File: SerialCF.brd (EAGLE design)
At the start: 101.6 x 34 mm, 4 parts, among them IC1 Z80CPU

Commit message: Finish Modularization
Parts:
- removed QG1: 6 MHz, crystal:DIL14S
- added LED1: AC, led:LED5MM
- added R1: 1k, eagle-ltspice:0207/10
- added R2: 560, resistor:0204/7
- added SV1: SERIAL, con-lstb:MA04-1
- added SV2: IDE PATA CF Card, con-lstb:MA20-2
- added V1, V2: 74HC00N, 74ttl-din:DIL14
- IC1: value Z80CPU -> XR-16C550P; device zilog:DIL40 -> exar:DIL40
- moved U$1 65.4 mm to (95.2, 12.7)
- moved IC1 31.9 mm to (34.3, 19.1), turned to 180 degrees
- moved JP1 1.27 mm to (73.7, 0.00)
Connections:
- removed net CLOCK: IC1.6, JP1.63, QG1.8
- removed net N$10: IC1.22, JP1.57
- removed net N$14: IC1.21, JP1.55
- removed net N$16: IC1.20, JP1.59
- removed net N$22: IC1.23, JP1.67
- removed net N$8: IC1.19, JP1.61
- removed net N$9: IC1.18, JP1.71
- new net !RD: IC1.21, SV2.25
- new net !WR: IC1.18, SV2.23
- new net +UB: V2.14
- new net -UB: V2.7
- new net IOCS1: SV2.37, V2.11
- new net N$11: IC1.11, SV1.1
- new net N$13: IC1.15, IC1.9
- new net N$15: IC1.10, SV1.2
- new net N$17: V1.13, V1.8
- new net N$18: IC1.14, V2.3
- new net N$19: JP1.59, V1.12, V1.2
- new net N$2: LED1.K, SV2.39
- new net N$20: R1.1, SV2.38
- new net N$3: LED1.A, R2.1
- new net N$4: V1.3, V2.2
- new net N$5: V2.1, V2.6
- new net N$6: V2.13, V2.8
- new net N$7: V1.11, V2.12
- new net RESET: IC1.35, V1.6
- net !RESET: now also SV2.1, V1.4, V1.5; no longer IC1.26
- net A0: now also IC1.28, SV2.35; no longer IC1.30
- net A1: now also IC1.27, SV2.33; no longer IC1.31
- net A10: no longer IC1.40
- net A11: no longer IC1.1
- net A12: no longer IC1.2
- net A13: no longer IC1.3
- net A14: no longer IC1.4
- net A15: no longer IC1.5
- net A2: now also IC1.26, SV2.36; no longer IC1.32
- net A3: no longer IC1.33
- net A4: no longer IC1.34
- net A5: no longer IC1.35
- net A6: now also V2.10, V2.4, V2.5, V2.9; no longer IC1.36
- net A7: now also V1.1, V1.10, V1.9; no longer IC1.37
- net A8: no longer IC1.38
- net A9: no longer IC1.39
- net D0: now also IC1.1, SV2.17; no longer IC1.14
- net D1: now also IC1.2, SV2.15; no longer IC1.15
- net D2: now also IC1.3, SV2.13; no longer IC1.12
- net D3: now also IC1.4, SV2.11; no longer IC1.8
- net D4: now also IC1.5, SV2.9; no longer IC1.7
- net D5: now also IC1.6, SV2.7; no longer IC1.9
- net D6: now also IC1.7, SV2.5; no longer IC1.10
- net D7: now also IC1.8, SV2.3; no longer IC1.13
- net GND: now also IC1.19, IC1.20, IC1.22, IC1.25, SV1.4, SV2.19, SV2.2, SV2.22, SV2.24, SV2.26, SV2.30, SV2.40, V1.7; no longer IC1.29, QG1.7
- net N$1: now also IC1.16, JP1.63; no longer IC1.27, JP1.75
- net VCC: now also IC1.12, IC1.13, IC1.37, IC1.38, IC1.39, IC1.40, R1.2, R2.2, SV1.3, SV2.20, V1.14; no longer IC1.11, IC1.16, IC1.17, IC1.25, JP1.69, JP1.73, JP1.77, QG1.14
- net WAIT: now also SV2.27; no longer IC1.24
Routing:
- net N$16: track 103.1 -> 0.00 mm, vias 1 -> 0
- net N$9: track 93.5 -> 0.00 mm, vias 1 -> 0
- net N$22: track 88.1 -> 0.00 mm
- net !RD: track 0.00 -> 87.0 mm, vias 0 -> 1
- net !WR: track 0.00 -> 83.0 mm, vias 0 -> 1
- net N$4: track 0.00 -> 78.9 mm, vias 0 -> 1
- net N$7: track 0.00 -> 74.7 mm, vias 0 -> 2
- net N$8: track 70.6 -> 0.00 mm, vias 1 -> 0
- net N$14: track 68.4 -> 0.00 mm, vias 2 -> 0
- net N$10: track 68.0 -> 0.00 mm, vias 2 -> 0
- net A7: track 28.0 -> 88.8 mm
- net N$19: track 0.00 -> 59.0 mm
- net D6: track 25.8 -> 84.7 mm, vias 0 -> 1
- net N$18: track 0.00 -> 57.4 mm, vias 0 -> 2
- net N$20: track 0.00 -> 57.1 mm, vias 0 -> 1
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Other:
- board size 101.6 x 34 mm -> 101.6 x 50.5 mm
- board text added: "+"
- board text added: "-"
- board text added: "CPD-80 Serial/CF V1"
- board text added: "RX"
- board text added: "TX"
- board text removed: "CPD-80 CPU V1"

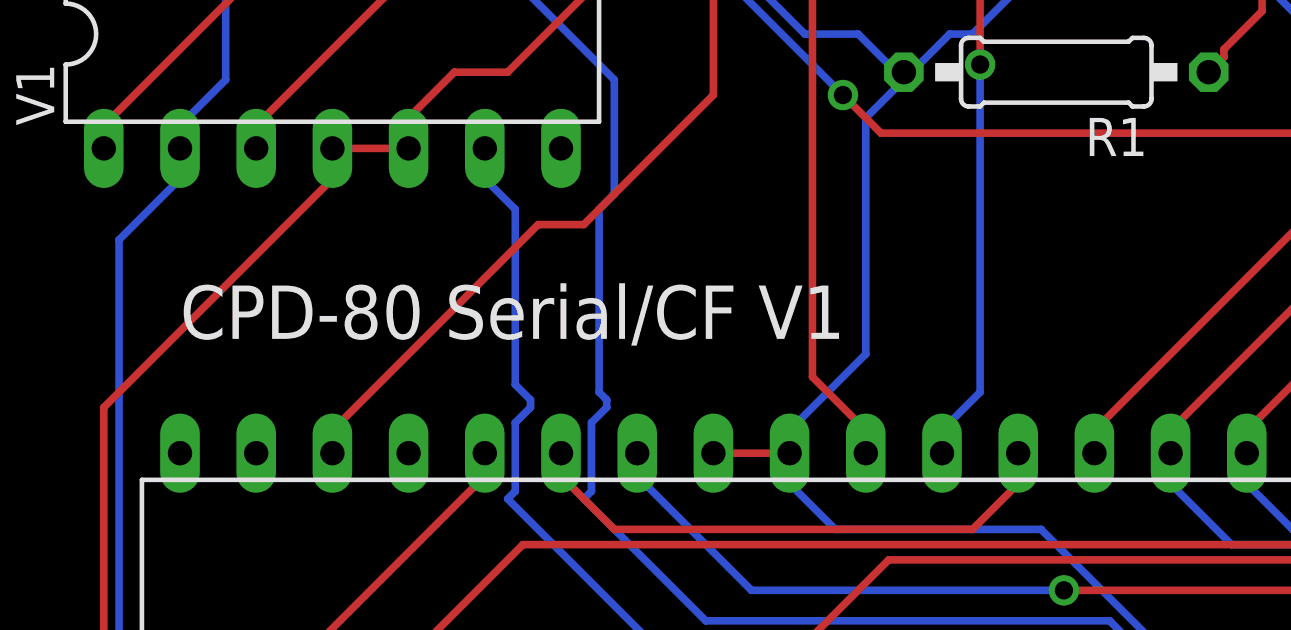
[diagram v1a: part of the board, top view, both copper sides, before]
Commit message: Update names and font
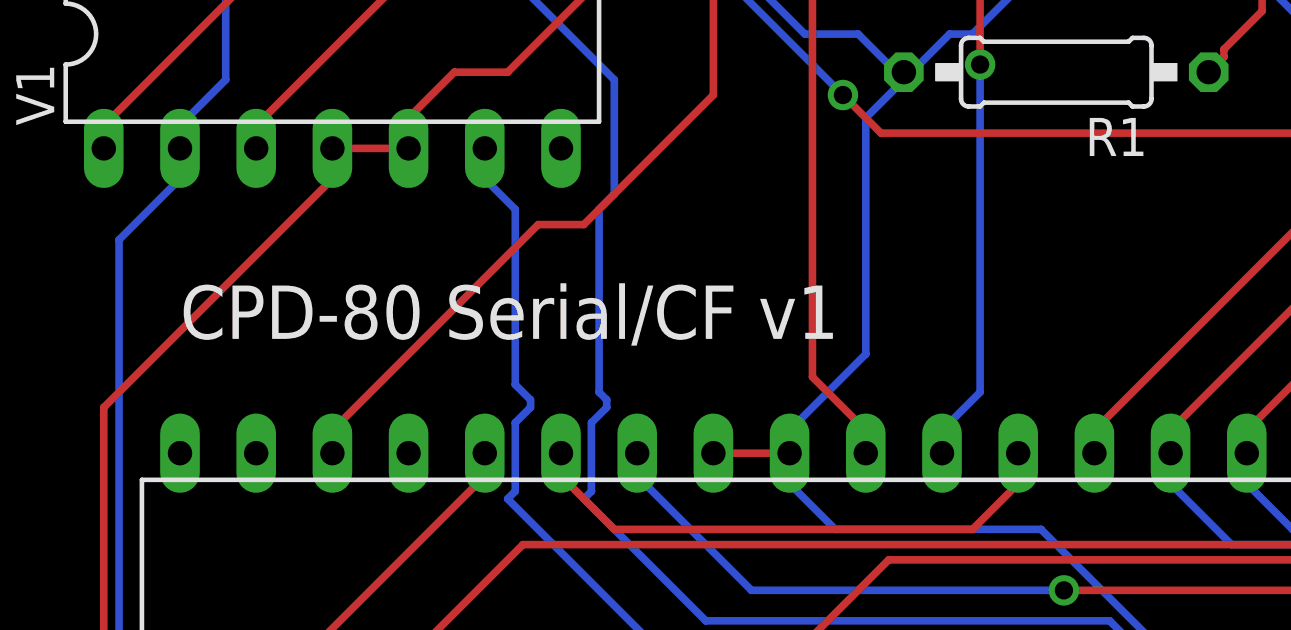
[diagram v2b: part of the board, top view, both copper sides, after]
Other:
- board text added: "CPD-80 Serial/CF v1"
- board text removed: "CPD-80 Serial/CF V1"
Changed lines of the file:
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@@
 <wire x1="104.12" y1="50.47" x2="2.54" y2="50.47" width="0" layer="20"/>
 <wire x1="2.54" y1="50.47" x2="2.54" y2="0" width="0" layer="20"/>
-<text x="33.02" y="48.26" size="1.778" layer="27">RX</text>
-<text x="35.56" y="48.26" size="1.778" layer="27">TX</text>
-<text x="38.735" y="48.26" size="1.778" layer="27">+</text>
-<text x="41.91" y="48.26" size="1.778" layer="27">-</text>
-<text x="10.16" y="30.48" size="1.778" layer="21">CPD-80 Serial/CF V1</text>
+<text x="33.02" y="48.26" size="1.524" layer="27" font="fixed">RX</text>
+<text x="36.195" y="48.26" size="1.524" layer="27" font="fixed">TX</text>
+<text x="39.37" y="48.26" size="1.524" layer="27" font="fixed">+</text>
+<text x="41.91" y="48.26" size="1.524" layer="27" font="fixed">-</text>
+<text x="10.16" y="30.48" size="1.778" layer="21" font="fixed">CPD-80 Serial/CF v1</text>
 <rectangle x1="50.5333" y1="30.5435" x2="50.8635" y2="30.5689" layer="21"/>
 <rectangle x1="50.3301" y1="30.5689" x2="50.9397" y2="30.5943" layer="21"/>

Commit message: Add Interrupt connection for 16550
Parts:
- added R3: 100k, resistor:0207/2V
- added R4: 3.3k, resistor:0207/2V
- added T1: BC547, transistor:TO92
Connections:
- new net N$10: IC1.30, R3.1
- new net N$8: R3.2, T1.2
- new net N$9: JP1.73, R4.1, T1.3
- net GND: now also T1.1
- net VCC: now also R4.2
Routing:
- net N$9: track 0.00 -> 68.7 mm, vias 0 -> 2
- net N$10: track 0.00 -> 34.7 mm, vias 0 -> 1
- net D1: track 74.3 -> 84.8 mm, vias 1 -> 3
- net N$8: track 0.00 -> 6.00 mm
- net VCC: track 185.7 -> 191.0 mm, vias 0 -> 1
- net N$18: track 57.4 -> 59.5 mm, vias 2 -> 3
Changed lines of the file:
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@@
 <element name="V2" library="74ttl-din" package="DIL14" value="74HC00N" x="80.01" y="31.75"/>
 <element name="U$1" library="bfl" package="OSHW2" value="" x="95.25" y="12.7"/>
+<element name="T1" library="transistor" package="TO92" value="BC547" x="71.12" y="17.78"/>
+<element name="R3" library="resistor" package="0207/2V" value="100k" x="64.77" y="21.59"/>
+<element name="R4" library="resistor" package="0207/2V" value="3.3k" x="63.5" y="16.51"/>
 </elements>
 <signals>
@@
 <wire x1="94.488" y1="22.352" x2="94.742" y2="22.352" width="0.254" layer="1"/>
 <wire x1="83.82" y1="11.684" x2="94.488" y2="22.352" width="0.254" layer="1"/>
-<wire x1="58.674" y1="11.684" x2="83.82" y2="11.684" width="0.254" layer="1"/>
+<wire x1="58.674" y1="11.684" x2="65.8368" y2="11.684" width="0.254" layer="1"/>
+<wire x1="65.8368" y1="11.684" x2="83.82" y2="11.684" width="0.254" layer="1"/>
 <wire x1="58.42" y1="11.43" x2="58.674" y2="11.684" width="0.254" layer="1"/>
 <wire x1="36.83" y1="6.604" x2="36.83" y2="6.35" width="0.254" layer="1"/>
@@
 <wire x1="30.48" y1="25.654" x2="32.004" y2="24.13" width="0.254" layer="16"/>
 <wire x1="30.48" y1="26.67" x2="30.48" y2="25.654" width="0.254" layer="16"/>
+<contactref element="R4" pad="2"/>
+<wire x1="64.9224" y1="16.002" x2="64.9224" y2="16.4592" width="0.254" layer="16"/>
+<wire x1="65.8368" y1="15.0876" x2="64.9224" y2="16.002" width="0.254" layer="16"/>
+<wire x1="65.8368" y1="13.0302" x2="65.8368" y2="15.0876" width="0.254" layer="16"/>
+<wire x1="65.8368" y1="11.684" x2="65.8368" y2="13.0302" width="0.254" layer="1"/>
+<wire x1="64.9224" y1="16.4592" x2="64.77" y2="16.51" width="0.254" layer="16"/>
+<wire x1="65.8368" y1="11.6586" x2="65.8368" y2="11.684" width="0.254" layer="1"/>
+<via x="65.8368" y="13.0302" extent="1-16" drill="0.6096"/>
 </signal>
 <signal name="GND">
@@
 <vertex x="104.14" y="49.53"/>
 </polygon>
+<contactref element="T1" pad="1"/>
 </signal>
 <signal name="A0">
@@
 <wire x1="91.694" y1="15.24" x2="100.33" y2="6.604" width="0.254" layer="16"/>
 <wire x1="74.676" y1="15.24" x2="91.694" y2="15.24" width="0.254" layer="16"/>
-<wire x1="66.294" y1="15.24" x2="74.676" y2="15.24" width="0.254" layer="1"/>
-<wire x1="55.88" y1="25.654" x2="66.294" y2="15.24" width="0.254" layer="1"/>
+<wire x1="66.294" y1="15.24" x2="73.3806" y2="15.24" width="0.254" layer="1"/>
+<wire x1="73.3806" y1="15.24" x2="74.676" y2="15.24" width="0.254" layer="1"/>
 <wire x1="55.88" y1="26.67" x2="55.88" y2="25.654" width="0.254" layer="1"/>
 <via x="74.676" y="15.24" extent="1-16" drill="0.6096"/>
+<wire x1="57.3786" y1="25.6032" x2="55.7784" y2="25.6032" width="0.254" layer="1"/>
+<wire x1="59.8932" y1="23.0886" x2="57.3786" y2="25.6032" width="0.254" layer="1"/>
+<wire x1="67.437" y1="23.0886" x2="59.8932" y2="23.0886" width="0.254" layer="1"/>
+<wire x1="67.6656" y1="22.86" x2="67.437" y2="23.0886" width="0.254" layer="1"/>
+<wire x1="69.4944" y1="21.0312" x2="67.6656" y2="22.86" width="0.254" layer="16"/>
+<wire x1="71.3232" y1="21.0312" x2="69.4944" y2="21.0312" width="0.254" layer="1"/>
+<wire x1="73.3806" y1="18.9738" x2="71.3232" y2="21.0312" width="0.254" layer="1"/>
+<wire x1="73.3806" y1="15.24" x2="73.3806" y2="18.9738" width="0.254" layer="1"/>
+<wire x1="55.7784" y1="25.6032" x2="55.88" y2="26.67" width="0.254" layer="1"/>
+<via x="67.6656" y="22.86" extent="1-16" drill="0.6096"/>
+<via x="69.4944" y="21.0312" extent="1-16" drill="0.6096"/>
 </signal>
 <signal name="D2">
@@
 <wire x1="39.624" y1="22.098" x2="29.21" y2="22.098" width="0.254" layer="16"/>
 <wire x1="58.166" y1="22.098" x2="39.624" y2="22.098" width="0.254" layer="1"/>
-<wire x1="72.644" y1="22.098" x2="58.166" y2="22.098" width="0.254" layer="16"/>
-<wire x1="77.47" y1="26.924" x2="72.644" y2="22.098" width="0.254" layer="16"/>
+<wire x1="77.47" y1="26.924" x2="73.1647" y2="22.6187" width="0.254" layer="16"/>
+<wire x1="73.1647" y1="22.6187" x2="72.644" y2="22.098" width="0.254" layer="16"/>
 <wire x1="77.47" y1="27.94" x2="77.47" y2="26.924" width="0.254" layer="16"/>
 <via x="39.624" y="22.098" extent="1-16" drill="0.6096"/>
 <via x="58.166" y="22.098" extent="1-16" drill="0.6096"/>
+<wire x1="72.2376" y1="23.5458" x2="73.1647" y2="22.6187" width="0.254" layer="16"/>
+<wire x1="72.009" y1="23.5458" x2="72.2376" y2="23.5458" width="0.254" layer="16"/>
+<wire x1="70.4088" y1="21.9456" x2="72.009" y2="23.5458" width="0.254" layer="16"/>
+<wire x1="67.2084" y1="21.9456" x2="70.4088" y2="21.9456" width="0.254" layer="1"/>
+<wire x1="66.5226" y1="22.6314" x2="67.2084" y2="21.9456" width="0.254" layer="1"/>
+<wire x1="58.7502" y1="22.6314" x2="66.5226" y2="22.6314" width="0.254" layer="1"/>
+<wire x1="58.293" y1="22.1742" x2="58.7502" y2="22.6314" width="0.254" layer="1"/>
+<wire x1="58.293" y1="22.1742" x2="58.166" y2="22.098" width="0.254" layer="1"/>
+<via x="70.4088" y="21.9456" extent="1-16" drill="0.6096"/>
 </signal>
 <signal name="N$17">
@@
 <via x="50.8" y="39.116" extent="1-16" drill="0.6096"/>
 </signal>
+<signal name="N$8">
+<contactref element="T1" pad="2"/>
+<contactref element="R3" pad="2"/>
+<wire x1="67.6656" y1="19.8882" x2="71.0946" y2="19.8882" width="0.254" layer="1"/>
+<wire x1="66.0654" y1="21.4884" x2="67.6656" y2="19.8882" width="0.254" layer="1"/>
+<wire x1="71.0946" y1="19.8882" x2="71.12" y2="19.685" width="0.254" layer="1"/>
+<wire x1="66.0654" y1="21.4884" x2="66.04" y2="21.59" width="0.254" layer="1"/>
+</signal>
+<signal name="N$9">
+<contactref element="T1" pad="3"/>
+<contactref element="R4" pad="1"/>
+<contactref element="JP1" pad="73"/>
+<wire x1="63.3222" y1="16.6878" x2="62.4078" y2="16.6878" width="0.254" layer="1"/>
+<wire x1="64.2366" y1="17.6022" x2="63.3222" y2="16.6878" width="0.254" layer="1"/>
+<wire x1="69.723" y1="17.6022" x2="64.2366" y2="17.6022" width="0.254" layer="1"/>
+<wire x1="62.4078" y1="16.6878" x2="62.23" y2="16.51" width="0.254" layer="1"/>
+<wire x1="69.723" y1="17.6022" x2="69.85" y2="17.78" width="0.254" layer="1"/>
+<wire x1="12.573" y1="6.1722" x2="11.43" y2="6.1722" width="0.254" layer="1"/>
+<wire x1="13.716" y1="5.0292" x2="12.573" y2="6.1722" width="0.254" layer="1"/>
+<wire x1="21.9456" y1="5.0292" x2="13.716" y2="5.0292" width="0.254" layer="1"/>
+<wire x1="22.86" y1="4.1148" x2="21.9456" y2="5.0292" width="0.254" layer="1"/>
+<wire x1="22.86" y1="3.429" x2="22.86" y2="4.1148" width="0.254" layer="1"/>
+<wire x1="23.7744" y1="2.5146" x2="22.86" y2="3.429" width="0.254" layer="1"/>
+<wire x1="29.4894" y1="2.5146" x2="23.7744" y2="2.5146" width="0.254" layer="1"/>
+<wire x1="30.6324" y1="3.6576" x2="29.4894" y2="2.5146" width="0.254" layer="1"/>
+<wire x1="30.6324" y1="4.3434" x2="30.6324" y2="3.6576" width="0.254" layer="1"/>
+<wire x1="31.5468" y1="5.2578" x2="30.6324" y2="4.3434" width="0.254" layer="1"/>
+<wire x1="32.2326" y1="5.2578" x2="31.5468" y2="5.2578" width="0.254" layer="1"/>
+<wire x1="33.147" y1="6.1722" x2="32.2326" y2="5.2578" width="0.254" layer="1"/>
+<wire x1="33.147" y1="6.858" x2="33.147" y2="6.1722" width="0.254" layer="1"/>
+<wire x1="35.6616" y1="9.3726" x2="33.147" y2="6.858" width="0.254" layer="1"/>
+<wire x1="37.0332" y1="10.7442" x2="35.6616" y2="9.3726" width="0.254" layer="16"/>
+<wire x1="37.0332" y1="12.573" x2="37.0332" y2="10.7442" width="0.254" layer="16"/>
+<wire x1="40.4622" y1="16.002" x2="37.0332" y2="12.573" width="0.254" layer="16"/>
+<wire x1="61.722" y1="16.002" x2="40.4622" y2="16.002" width="0.254" layer="1"/>
+<wire x1="62.23" y1="16.51" x2="61.722" y2="16.002" width="0.254" layer="1"/>
+<wire x1="11.43" y1="6.1722" x2="11.43" y2="6.35" width="0.254" layer="1"/>
+<via x="35.6616" y="9.3726" extent="1-16" drill="0.6096"/>
+<via x="40.4622" y="16.002" extent="1-16" drill="0.6096"/>
+</signal>
+<signal name="N$10">
+<contactref element="R3" pad="1"/>
+<contactref element="IC1" pad="30"/>
+<wire x1="39.0906" y1="17.3736" x2="33.147" y2="11.43" width="0.254" layer="16"/>
+<wire x1="59.2074" y1="17.3736" x2="39.0906" y2="17.3736" width="0.254" layer="1"/>
+<wire x1="63.3222" y1="21.4884" x2="59.2074" y2="17.3736" width="0.254" layer="1"/>
+<wire x1="33.147" y1="11.43" x2="33.02" y2="11.43" width="0.254" layer="16"/>
+<wire x1="63.3222" y1="21.4884" x2="63.5" y2="21.59" width="0.254" layer="1"/>
+<via x="39.0906" y="17.3736" extent="1-16" drill="0.6096"/>
+</signal>
 </signals>
